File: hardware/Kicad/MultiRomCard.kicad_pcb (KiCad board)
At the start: 2 copper layers, 0 parts

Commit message: Preparations for PCB layout
- Created footprints for Cartridge Bus and Arduino UNO,
- Modified Arduino UNO schematic symbol to include pin numbers,
- Created initial netlist, and
- Spread all footprints on board, no traces yet.
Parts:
- added P1: VC4000_Cartridge_Bus, VC4000_MultiRom:VC4000_CartridgeBus, F.Cu at (131.8, 74.8)
- added U1: Arduino_UNO, VC4000_MultiRom:Arduino_UNO, F.Cu at (131.1, 107.3)
- added U2: 74HC595, Housings_DIP:DIP-16__300_ELL, F.Cu at (180.0, 120.5)
- added U3: 74HC595, Housings_DIP:DIP-16__300_ELL, F.Cu at (180.0, 130.9)
- added U4: 74HC595, Housings_DIP:DIP-16__300_ELL, F.Cu at (203.6, 120.5)
- added U5: 6264, Housings_DIP:DIP-28__600_ELL, F.Cu at (190.3, 75.1)
- added U6: 74HC245, Housings_DIP:DIP-20__300_ELL, F.Cu at (182.6, 89.3)
- added U7: 74HC245, Housings_DIP:DIP-20__300_ELL, F.Cu at (182.6, 99.7)
- added U8: 74HC245, Housings_DIP:DIP-20__300_ELL, F.Cu at (182.6, 110.1)

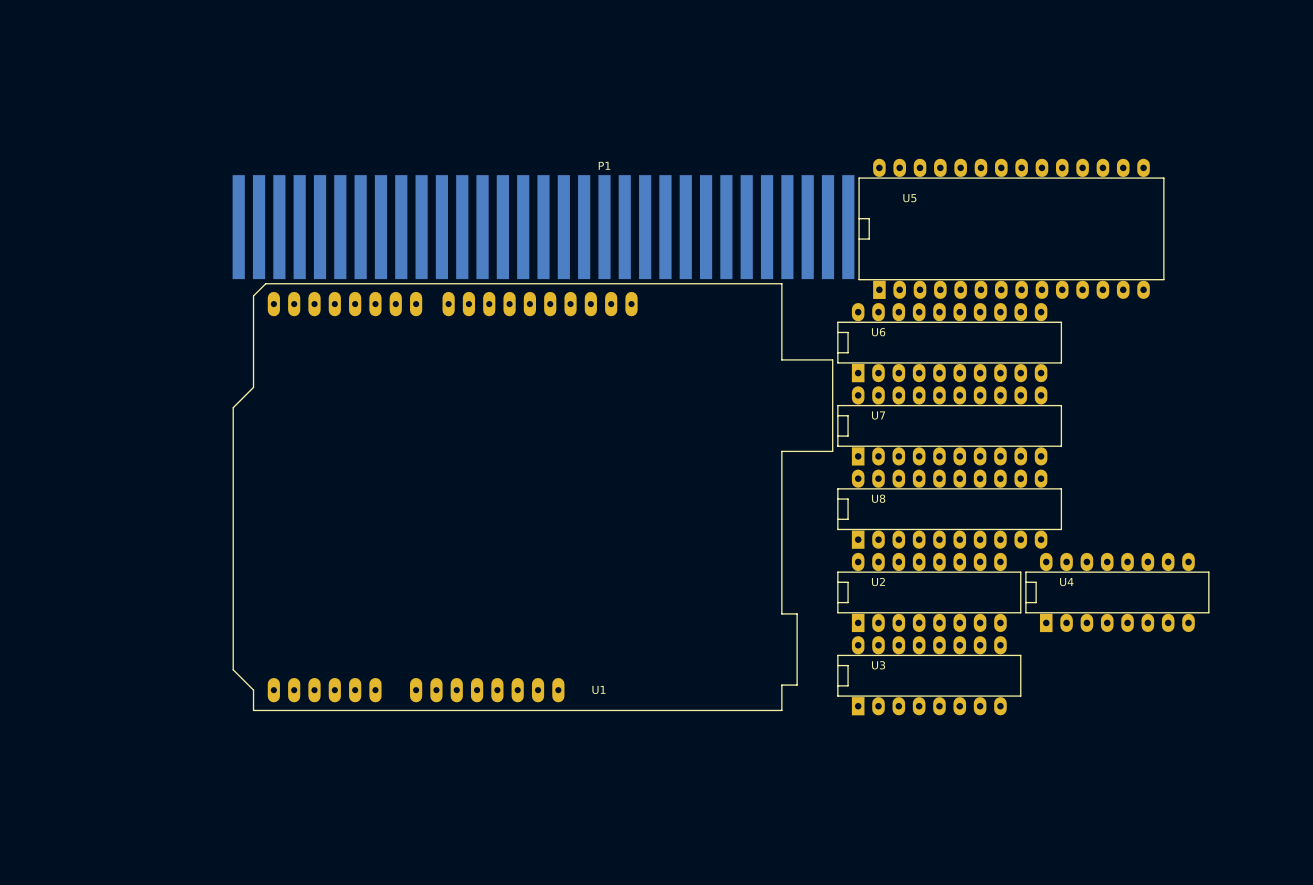
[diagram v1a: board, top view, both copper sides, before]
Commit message: Euro PCB outline and some part changes (BREAKS CURRENT FIRMWARE!)
- Swapped A and B sides on Bus transcievers for easier tracing.
  (Not sure if this is ideal, yet, but certainly better than
  before!). THIS BREAKS CURRENT FIRMWARE! Need to change
  direction bits!
- Prefix bus labels from the cartridge to the transcievers with 'E'
  (for 'external') to de-confuse Pcbnew.
- Connect second +5V and GND connectors to power nets for easier
  board connections.
- revert previous changes to cartridge bus footprint.
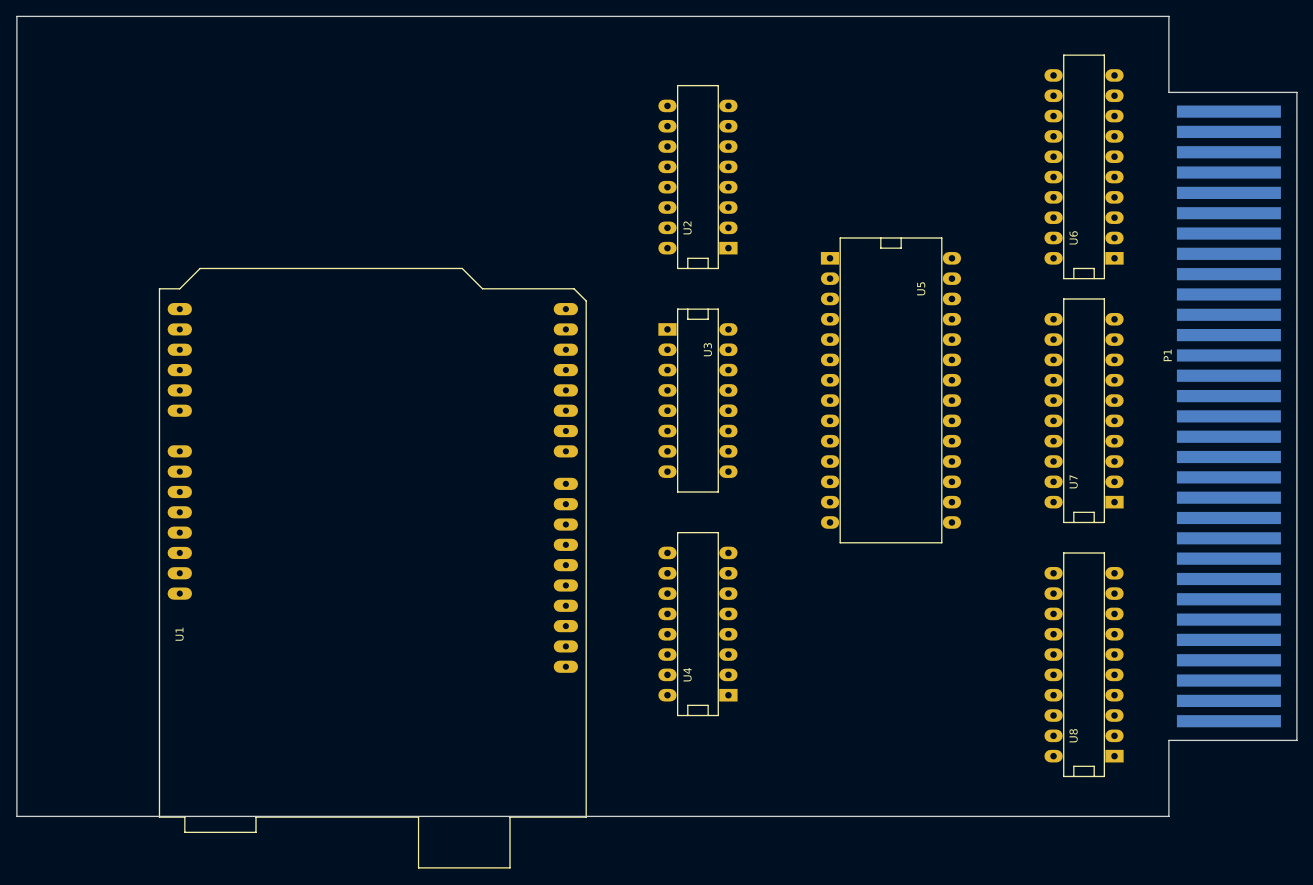
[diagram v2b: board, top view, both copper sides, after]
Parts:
- P1: footprint VC4000_MultiRom:VC4000_CartridgeBus -> VC4000_CartridgeBus
- moved P1 88.9 mm to (217.5, 98.5), turned to 90 degrees
- moved U2 59.4 mm to (151.1, 68.6), turned to 90 degrees
- moved U4 52.6 mm to (151.1, 124.5), turned to 90 degrees
- moved U3 44.9 mm to (151.1, 96.5), turned to 270 degrees
- moved U6 27.7 mm to (199.4, 67.3), turned to 90 degrees
- moved U8 25.7 mm to (199.4, 129.5), turned to 90 degrees
- moved U5 25.2 mm to (175.3, 95.2), turned to 270 degrees
- moved U1 22.2 mm to (111.8, 118.1), turned to 270 degrees
- moved U7 16.9 mm to (199.4, 97.8), turned to 90 degrees
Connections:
- P1 pad 1: /D0 -> /ED0
- P1 pad 10: /A11 -> /EA11
- P1 pad 11: /A10 -> /EA10
- P1 pad 15: /A9 -> /EA9
- P1 pad 16: /A8 -> /EA8
- P1 pad 18: /A0 -> /EA0
- P1 pad 19: /A1 -> /EA1
- P1 pad 2: /D1 -> /ED1
- P1 pad 20: /A2 -> /EA2
- P1 pad 21: /A3 -> /EA3
- P1 pad 22: /A4 -> /EA4
- P1 pad 23: /A5 -> /EA5
- P1 pad 24: /A6 -> /EA6
- P1 pad 25: /A7 -> /EA7
- P1 pad 29: Net-(P1-Pad29) -> GND
- P1 pad 3: /D2 -> /ED2
- P1 pad 30: Net-(P1-Pad30) -> VCC
- P1 pad 5: /D3 -> /ED3
- P1 pad 6: /D4 -> /ED4
- P1 pad 7: /D5 -> /ED5
- P1 pad 8: /D6 -> /ED6
- P1 pad 9: /D7 -> /ED7
- U6 pad 2: /A0 -> /EA0
- U6 pad 3: /A1 -> /EA1
- U6 pad 4: /A2 -> /EA2
- U6 pad 5: /A3 -> /EA3
- U6 pad 6: /A4 -> /EA4
- U6 pad 7: /A5 -> /EA5
- U6 pad 8: /A6 -> /EA6
- U6 pad 9: /A7 -> /EA7
- U7 pad 11: Net-(U7-Pad11) -> /A8
- U7 pad 12: GND -> /A9
- U7 pad 13: Net-(P1-Pad12) -> /A10
- U7 pad 14: GND -> /A11
- U7 pad 15: /A11 -> /A12
- U7 pad 16: /A10 -> CE2SRAM
- U7 pad 17: /A9 -> CE1SRAM
- U7 pad 18: /A8 -> Net-(U7-Pad18)
- U7 pad 2: /A8 -> Net-(U7-Pad2)
- U7 pad 3: /A9 -> GND
- U7 pad 4: /A10 -> Net-(P1-Pad12)
- U7 pad 5: /A11 -> GND
- U7 pad 6: /A12 -> /EA11
- U7 pad 7: CE2SRAM -> /EA10
- U7 pad 8: CE1SRAM -> /EA9
- U7 pad 9: Net-(U7-Pad9) -> /EA8
- U8 pad 2: /D0 -> /ED0
- U8 pad 3: /D1 -> /ED1
- U8 pad 4: /D2 -> /ED2
- U8 pad 5: /D3 -> /ED3
- U8 pad 6: /D4 -> /ED4
- U8 pad 7: /D5 -> /ED5
- U8 pad 8: /D6 -> /ED6
- U8 pad 9: /D7 -> /ED7
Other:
- board outline added: 160 x 100 mm
- net class Default: clearance 0.254 -> 0.4; trace_width 0.254 -> 0.5
- rule trace_clearance: 0.254 -> 0.4

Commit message: Move "CE2" track to another BT pin and remove special.lib.
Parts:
- moved U1 17.9 mm to (93.9, 118.0)
- moved U2 6.39 mm to (151.4, 62.2)
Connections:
- U7 pad 13: /A10 -> CE2SRAM
- U7 pad 14: /A11 -> /A10
- U7 pad 15: /A12 -> /A11
- U7 pad 16: CE2SRAM -> /A12
- U7 pad 4: Net-(P1-Pad12) -> GND
- U7 pad 5: GND -> /EA11
- U7 pad 6: /EA11 -> /EA10
- U7 pad 7: /EA10 -> Net-(P1-Pad12)
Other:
- net class Default: clearance 0.4 -> 0.75; trace_width 0.5 -> 1
- rule trace_clearance: 0.4 -> 0.75
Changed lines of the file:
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@@
-(kicad_pcb (version 4) (host pcbnew "(2015-04-25 BZR 5623)-product")
+(kicad_pcb (version 4) (host pcbnew "(2015-05-05 BZR 5645)-product")
   (general
     (links 111)
     (no_connects 111)
-    (area 65.949999 48.449999 226.050001 155.205001)
+    (area 65.949999 48.449999 226.050001 148.550001)
     (thickness 1.6)
     (drawings 8)
@@
   )
   (setup
-    (last_trace_width 0.5)
-    (trace_clearance 0.4)
+    (last_trace_width 1)
+    (trace_clearance 0.75)
     (zone_clearance 0.508)
     (zone_45_only no)
@@
   (net 83 "Net-(U7-Pad18)")
   (net_class Default "This is the default net class."
-    (clearance 0.4)
-    (trace_width 0.5)
+    (clearance 0.75)
+    (trace_width 1)
     (via_dia 0.889)
     (via_drill 0.635)
@@
   )
   (module VC4000_MultiRom:Arduino_UNO (layer F.Cu)
-    (at 111.76 118.11 270)
+    (at 93.9 118 270)
     (fp_text reference U1 (at 7.62 25.4 270) (layer F.SilkS)
       (effects (font (size 1 1) (thickness 0.15)))
@@
   )
   (module Housings_DIP:DIP-16__300_ELL (layer F.Cu)
-    (at 151.13 68.58 90)
+    (at 151.4 62.2 90)
     (descr "16 pins DIL package, elliptical pads")
     (tags DIL)
@@
       (net 25 GND))
     (pad 4 thru_hole oval (at -3.81 3.81 90) (size 1.5748 2.286) (drill 0.8128) (layers *.Cu *.Mask F.SilkS)
+      (net 25 GND))
+    (pad 5 thru_hole oval (at -1.27 3.81 90) (size 1.5748 2.286) (drill 0.8128) (layers *.Cu *.Mask F.SilkS)
+      (net 73 /EA11))
+    (pad 6 thru_hole oval (at 1.27 3.81 90) (size 1.5748 2.286) (drill 0.8128) (layers *.Cu *.Mask F.SilkS)
+      (net 72 /EA10))
+    (pad 7 thru_hole oval (at 3.81 3.81 90) (size 1.5748 2.286) (drill 0.8128) (layers *.Cu *.Mask F.SilkS)
       (net 17 "Net-(P1-Pad12)"))
-    (pad 5 thru_hole oval (at -1.27 3.81 90) (size 1.5748 2.286) (drill 0.8128) (layers *.Cu *.Mask F.SilkS)
-      (net 25 GND))
-    (pad 6 thru_hole oval (at 1.27 3.81 90) (size 1.5748 2.286) (drill 0.8128) (layers *.Cu *.Mask F.SilkS)
-      (net 73 /EA11))
-    (pad 7 thru_hole oval (at 3.81 3.81 90) (size 1.5748 2.286) (drill 0.8128) (layers *.Cu *.Mask F.SilkS)
-      (net 72 /EA10))
     (pad 8 thru_hole oval (at 6.35 3.81 90) (size 1.5748 2.286) (drill 0.8128) (layers *.Cu *.Mask F.SilkS)
       (net 71 /EA9))
@@
       (net 15 /A9))
     (pad 13 thru_hole oval (at 6.35 -3.81 90) (size 1.5748 2.286) (drill 0.8128) (layers *.Cu *.Mask F.SilkS)
+      (net 35 CE2SRAM))
+    (pad 14 thru_hole oval (at 3.81 -3.81 90) (size 1.5748 2.286) (drill 0.8128) (layers *.Cu *.Mask F.SilkS)
       (net 18 /A10))
-    (pad 14 thru_hole oval (at 3.81 -3.81 90) (size 1.5748 2.286) (drill 0.8128) (layers *.Cu *.Mask F.SilkS)
+    (pad 15 thru_hole oval (at 1.27 -3.81 90) (size 1.5748 2.286) (drill 0.8128) (layers *.Cu *.Mask F.SilkS)
       (net 19 /A11))
-    (pad 15 thru_hole oval (at 1.27 -3.81 90) (size 1.5748 2.286) (drill 0.8128) (layers *.Cu *.Mask F.SilkS)
+    (pad 16 thru_hole oval (at -1.27 -3.81 90) (size 1.5748 2.286) (drill 0.8128) (layers *.Cu *.Mask F.SilkS)
       (net 55 /A12))
-    (pad 16 thru_hole oval (at -1.27 -3.81 90) (size 1.5748 2.286) (drill 0.8128) (layers *.Cu *.Mask F.SilkS)
-      (net 35 CE2SRAM))
     (pad 17 thru_hole oval (at -3.81 -3.81 90) (size 1.5748 2.286) (drill 0.8128) (layers *.Cu *.Mask F.SilkS)
       (net 36 CE1SRAM))

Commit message: Move footprints a little.
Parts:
- moved U4 16.1 mm to (135.1, 122.9)
- moved U3 16.1 mm to (135.1, 95.0)
- moved U2 16.0 mm to (135.5, 64.0)
- moved U5 11.3 mm to (164.3, 92.6)
- moved U6 8.11 mm to (191.3, 66.7)
- moved U8 8.08 mm to (191.5, 127.8)
- moved U7 8.02 mm to (191.4, 97.2)
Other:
- net class Default: clearance 0.75 -> 0.5; trace_width 1 -> 0.75; via_dia 0.889 -> 1.5; via_drill 0.635 -> 0.75
- rule trace_clearance: 0.75 -> 0.5
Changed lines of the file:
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@@
     (links 111)
     (no_connects 111)
-    (area 65.949999 48.449999 226.050001 148.550001)
+    (area 65.134999 48.449999 226.050001 155.655001)
     (thickness 1.6)
     (drawings 8)
@@
   )
   (setup
-    (last_trace_width 1)
-    (trace_clearance 0.75)
+    (last_trace_width 0.75)
+    (trace_clearance 0.5)
     (zone_clearance 0.508)
     (zone_45_only no)
@@
     (segment_width 0.2)
     (edge_width 0.1)
-    (via_size 0.889)
-    (via_drill 0.635)
+    (via_size 1.5)
+    (via_drill 0.75)
     (via_min_size 0.889)
     (via_min_drill 0.508)
@@
   (net 83 "Net-(U7-Pad18)")
   (net_class Default "This is the default net class."
-    (clearance 0.75)
-    (trace_width 1)
-    (via_dia 0.889)
-    (via_drill 0.635)
+    (clearance 0.5)
+    (trace_width 0.75)
+    (via_dia 1.5)
+    (via_drill 0.75)
     (uvia_dia 0.508)
     (uvia_drill 0.127)
@@
   )
   (module Housings_DIP:DIP-16__300_ELL (layer F.Cu)
-    (at 151.4 62.2 90)
+    (at 135.49 63.95 90)
     (descr "16 pins DIL package, elliptical pads")
     (tags DIL)
@@
   )
   (module Housings_DIP:DIP-16__300_ELL (layer F.Cu)
-    (at 151.13 96.52 270)
+    (at 135.09 95.05 270)
     (descr "16 pins DIL package, elliptical pads")
     (tags DIL)
@@
   )
   (module Housings_DIP:DIP-16__300_ELL (layer F.Cu)
-    (at 151.13 124.46 90)
+    (at 135.09 122.91 90)
     (descr "16 pins DIL package, elliptical pads")
     (tags DIL)
@@
   )
   (module Housings_DIP:DIP-28__600_ELL (layer F.Cu)
-    (at 175.26 95.25 270)
+    (at 164.3 92.6 270)
     (descr "28 pins DIL package, elliptical pads, width 600mil")
     (tags DIL)
@@
   )
   (module Housings_DIP:DIP-20__300_ELL (layer F.Cu)
-    (at 199.39 67.31 90)
+    (at 191.3 66.7 90)
     (descr "20 pins DIL package, elliptical pads")
     (tags DIL)
@@
   )
   (module Housings_DIP:DIP-20__300_ELL (layer F.Cu)
-    (at 199.39 97.79 90)
+    (at 191.39 97.19 90)
     (descr "20 pins DIL package, elliptical pads")
     (tags DIL)
@@
   )
   (module Housings_DIP:DIP-20__300_ELL (layer F.Cu)
-    (at 199.39 129.54 90)
+    (at 191.51 127.75 90)
     (descr "20 pins DIL package, elliptical pads")
     (tags DIL)

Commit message: First attempt at routing.
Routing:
- net VCC: track 0.00 -> 323.4 mm, vias 0 -> 10
- net GND: track 0.00 -> 215.1 mm, vias 0 -> 6
- net /A11: track 0.00 -> 205.5 mm, vias 0 -> 8
- net OEVCBUS: track 0.00 -> 203.7 mm, vias 0 -> 4
- net CE1SRAM: track 0.00 -> 175.7 mm, vias 0 -> 4
- net /A9: track 0.00 -> 156.0 mm, vias 0 -> 4
- net /A12: track 0.00 -> 152.9 mm, vias 0 -> 6
- net /A10: track 0.00 -> 136.8 mm, vias 0 -> 8
- net Net-(U1-Pad5): track 0.00 -> 119.5 mm, vias 0 -> 2
- net Net-(U1-Pad28): track 0.00 -> 118.3 mm, vias 0 -> 4
- net CE2SRAM: track 0.00 -> 112.3 mm, vias 0 -> 6
- net /A0: track 0.00 -> 103.6 mm, vias 0 -> 2
- net /D0: track 0.00 -> 103.3 mm
- net Net-(U1-Pad4): track 0.00 -> 101.0 mm
- net /D1: track 0.00 -> 84.0 mm, vias 0 -> 2
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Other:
- net class Power added: clearance 1, trace_width 1.5, via_dia 3, via_drill 1.5

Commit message: [PCB] First version with all nets connected.
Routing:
- net GND: track 215.1 -> 371.0 mm, vias 6 -> 13
- net VCC: track 323.4 -> 432.1 mm, vias 10 -> 20
- net /A8: track 16.5 -> 92.3 mm, vias 0 -> 4
- net Net-(U1-Pad5): track 119.5 -> 96.8 mm
- net Net-(P1-Pad13): track 0.00 -> 17.8 mm
- net /A12: track 152.9 -> 135.4 mm, vias 6 -> 8
- net CE2SRAM: track 112.3 -> 126.9 mm, vias 6 -> 8
- net /A10: track 136.8 -> 128.2 mm
- net Net-(U1-Pad4): track 101.0 -> 94.9 mm
- net /A9: track 156.0 -> 160.7 mm
- net WESRAM: track 77.0 -> 74.8 mm
- net /A11: track 205.5 -> 207.4 mm
- net /D1: track 84.0 -> 85.7 mm
- net OEVCBUS: track 203.7 -> 205.2 mm
- net /A0: track 103.6 -> 104.5 mm
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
